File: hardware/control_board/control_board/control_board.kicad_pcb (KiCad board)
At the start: 4 copper layers, 140 parts, among them J1 USB_B, J2 Conn_02x08_Counter_Clockwise, J3 Conn_01x06_Pin, J4 Barrel_Jack_Switch, Q1 SS8550, Q2 AO3401A, SW1 SW_MEC_5G, SW2 SW_MEC_5G, U1 STM32F411CEUx, U2 M24C64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

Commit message: feat：调试接口预布局；USB接口预布局
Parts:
- added D9: 1N4007, Diode_SMD:D_SOD-123, F.Cu at (121.3, 43.7)
- added R30: 4.7kR, Resistor_SMD:R_0603_1608Metric, F.Cu at (117.7, 39.4)
- added R31: 4.7kR, Resistor_SMD:R_0603_1608Metric, F.Cu at (119.2, 39.4)
- TP11: value +1V -> +3.3V
- moved Q2 138.4 mm to (119.7, 93.6), turned to 180 degrees
- moved D3 135.4 mm to (122.9, 93.6), turned to -90 degrees
- moved BT1 133.0 mm to (110.5, 108.5), turned to -90 degrees
- moved R4 131.2 mm to (122.9, 97.5), turned to 90 degrees
- moved R10 117.7 mm to (154.9, 40.2)
- moved R11 117.7 mm to (154.9, 38.7)
- moved R9 117.7 mm to (154.9, 41.6)
- moved U2 117.7 mm to (149.3, 39.5)
- moved C6 117.7 mm to (151.0, 35.8)
- moved R8 106.6 mm to (176.9, 101.4)
- moved SW1 106.6 mm to (176.9, 94.9)
- moved C10 105.6 mm to (154.6, 107.4)
- moved C11 105.6 mm to (143.3, 102.2)
- moved C2 105.6 mm to (140.8, 114.1)
- moved C4 105.6 mm to (137.3, 106.3)
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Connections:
- D2 pad 1: GND -> /MCU/Debug_LED
- D2 pad 2: /MCU/Debug_LED -> Net-(D2-A)
- Q1 pad 1: /MCU/Buzzer -> Net-(Q1-B)
- R3 pad 1: /MCU/Debug_LED -> Net-(D2-A)
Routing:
- net /USB_D.USB_D+: track 0.00 -> 10.0 mm
- net /USB_D.USB_D-: track 0.00 -> 8.67 mm
- net VBUS: track 0.00 -> 1.63 mm
- net /USB_D.VBUS_Check: track 0.00 -> 1.49 mm

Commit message: feat：电源预布局
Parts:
- added J5: Conn_01x08, Connector_JST:JST_VH_B8P-VH_1x08_P3.96mm_Vertical, F.Cu at (37.0, 113.6)
- moved R26 130.1 mm to (-48.6, 53.0), turned to -90 degrees
- moved R24 129.6 mm to (-48.5, 49.2), turned to 90 degrees
- moved R27 128.4 mm to (-47.1, 56.4), turned to 90 degrees
- moved R25 128.2 mm to (-48.6, 56.0), turned to -90 degrees
- moved R22 121.2 mm to (-48.2, 94.5), turned to -90 degrees
- moved C50 120.8 mm to (-45.1, 46.6)
- moved R23 119.7 mm to (-46.7, 97.9), turned to 90 degrees
- moved C51 119.4 mm to (-42.1, 46.6), turned to 180 degrees
- moved R20 118.1 mm to (-48.1, 90.7), turned to 90 degrees
- moved R21 117.7 mm to (-48.2, 97.5), turned to -90 degrees
- moved C59 116.7 mm to (-44.9, 57.2)
- moved D2 116.7 mm to (190.3, 75.1)
- moved R3 116.7 mm to (193.6, 75.1)
- moved C58 116.4 mm to (-44.9, 55.7)
- moved C53 116.2 mm to (-49.3, 72.3)
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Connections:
- C15 pad 1: +17V -> V_{IN}
- C16 pad 2: +17V -> V_{IN}
- C17 pad 2: +17V -> V_{IN}
- C18 pad 2: +17V -> V_{IN}
- C37 pad 1: +17V -> V_{IN}
- C38 pad 2: +17V -> V_{IN}
- C39 pad 2: +17V -> V_{IN}
- C40 pad 2: +17V -> V_{IN}
- C41 pad 2: +17V -> V_{IN}
- C61 pad 2: +17V -> V_{IN}
- C62 pad 2: +17V -> V_{IN}
- C63 pad 2: +17V -> V_{IN}
- U3 pad 2: +17V -> V_{IN}
- U5 pad 2: +17V -> V_{IN}
- U7 pad 3: +17V -> V_{IN}
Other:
- board outline added: 100 x 100 mm

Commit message: feat：整版布局
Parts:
- C6, R10, R11, R9, U2: moved to B.Cu
- TP1: value SPI_CS -> CS
- TP2: value SPI_CLK -> CLK
- TP3: value SPI_MISO -> MISO
- TP4: value SPI_MOSI -> MOSI
- TP5: value IIC_SCL -> SCL
- TP6: value IIC_SDA -> SDA
- moved C5 134.5 mm to (110.7, 90.1), turned to 90 degrees
- moved SW2 132.3 mm to (111.6, 96.6), turned to 90 degrees
- moved R7 131.5 mm to (112.2, 90.1), turned to 90 degrees
- moved R10 131.2 mm to (92.6, 77.3), turned to 180 degrees
- moved R11 131.2 mm to (92.6, 75.8), turned to 180 degrees
- moved R9 131.2 mm to (92.6, 78.8), turned to 180 degrees
- moved R8 130.3 mm to (116.2, 90.1), turned to -90 degrees
- moved J3 129.5 mm to (83.2, 65.4)
- moved SW1 128.3 mm to (116.2, 96.5), turned to -90 degrees
- moved C6 123.5 mm to (96.5, 73.0), turned to 0 degrees
- moved C9 121.7 mm to (100.4, 86.0)
- moved C8 121.7 mm to (99.4, 85.0)
- moved C11 121.6 mm to (93.2, 88.7)
- moved C13 121.6 mm to (96.2, 97.0)
- moved R5 121.6 mm to (100.4, 99.1)
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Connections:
- U1 pad 31: /MCU/VBUS_Check -> /USB_D.VBUS_Check
- U1 pad 32: /MCU/USB_D- -> /USB_D.USB_D-
- U1 pad 33: /MCU/USB_D+ -> /USB_D.USB_D+
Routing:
- net /USB_D.USB_D-: track 8.67 -> 3.30 mm
- net /USB_D.USB_D+: track 10.0 -> 8.10 mm

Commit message: feat：MCU、USB、EEPROM、Debug布线
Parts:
- SW1: value SW_MEC_5G -> BOOT0
- SW2: value SW_MEC_5G -> NRST
- moved R30 15.6 mm to (111.2, 66.0)
- moved R31 15.6 mm to (111.2, 64.5)
- moved BZ1 15.6 mm to (111.2, 56.4)
- moved Q1 15.6 mm to (111.2, 61.7)
- moved D9 15.5 mm to (114.5, 62.5)
- moved R3 13.1 mm to (116.3, 73.5)
- moved D2 12.5 mm to (116.3, 75.0), turned to 180 degrees
- moved C5 11.4 mm to (115.7, 79.8)
- moved R7 11.4 mm to (117.2, 79.8)
- moved SW2 11.4 mm to (116.5, 86.3)
- moved R8 3.11 mm to (116.6, 93.2)
- moved SW1 3.11 mm to (116.6, 99.6)
- moved C23 2.23 mm to (32.6, 32.7)
- moved C25 2.23 mm to (27.7, 29.0)
- moved C26 2.23 mm to (27.7, 26.6)
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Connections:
- C61 pad 2: V_{IN} -> +17V
- C62 pad 2: V_{IN} -> +17V
- C63 pad 2: V_{IN} -> +17V
- U7 pad 3: V_{IN} -> +17V
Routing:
- net /MCU/NRST: track 0.00 -> 79.3 mm, vias 0 -> 2
- net /USB_D.USB_D-: track 3.30 -> 63.3 mm
- net /USB_D.USB_D+: track 8.10 -> 63.4 mm
- net /USB_D.VBUS_Check: track 1.49 -> 56.8 mm, vias 0 -> 2
- net /MCU/BOOT0: track 0.00 -> 33.8 mm, vias 0 -> 2
- net /MCU/Debug_RX: track 0.00 -> 31.2 mm, vias 0 -> 1
- net /MCU/Debug_TX: track 0.00 -> 29.8 mm, vias 0 -> 1
- net /MCU/SWDIO: track 0.00 -> 29.7 mm, vias 0 -> 1
- net /MCU/SWCLK: track 0.00 -> 29.1 mm, vias 0 -> 1
- net /MCU/Buzzer: track 0.00 -> 28.8 mm
- net /FPGA_Ctrl.Ctrl_SPI_CS: track 0.00 -> 24.7 mm
- net /FPGA_Ctrl.Ctrl_SPI_MISO: track 0.00 -> 24.5 mm
- net /FPGA_Ctrl.Ctrl_FPGA_NRST: track 0.00 -> 22.5 mm
- net /MCU/Debug_LED: track 0.00 -> 22.4 mm
- net +3.3V: track 2.32 -> 24.5 mm, vias 0 -> 9
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- added copper zone on F.Cu, net +3.3V
- added copper zone on B.Cu, net GND
- added copper zone on F.Cu, net GND
- added copper zone on In1.Cu, net GND
- added copper zone on F.Cu, net Net-(BT1-+)
- added copper zone on F.Cu, net Net-(BZ1-+)
- added copper zone on F.Cu, net Net-(D3-K)
- added copper zone on In2.Cu, net Net-(D3-K)
- added copper zone on F.Cu, net VBUS

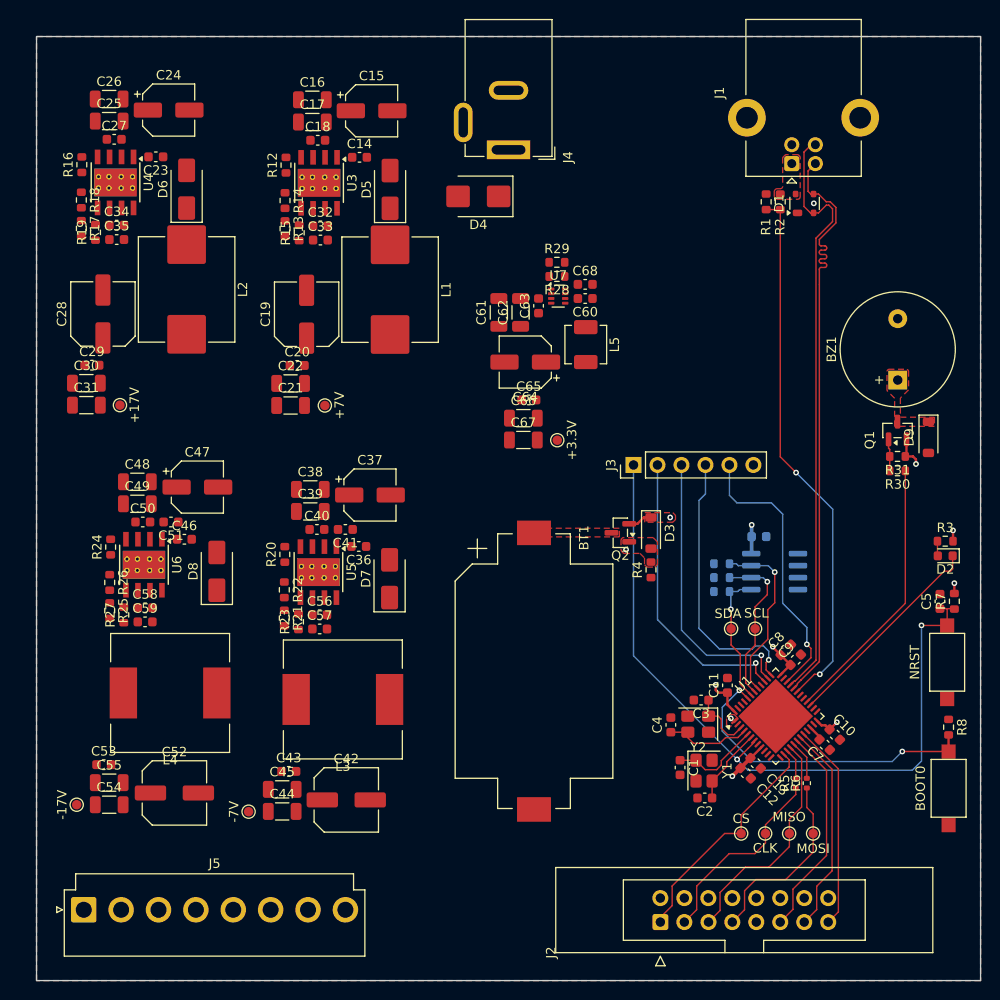
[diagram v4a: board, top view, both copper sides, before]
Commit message: feat：电源布线
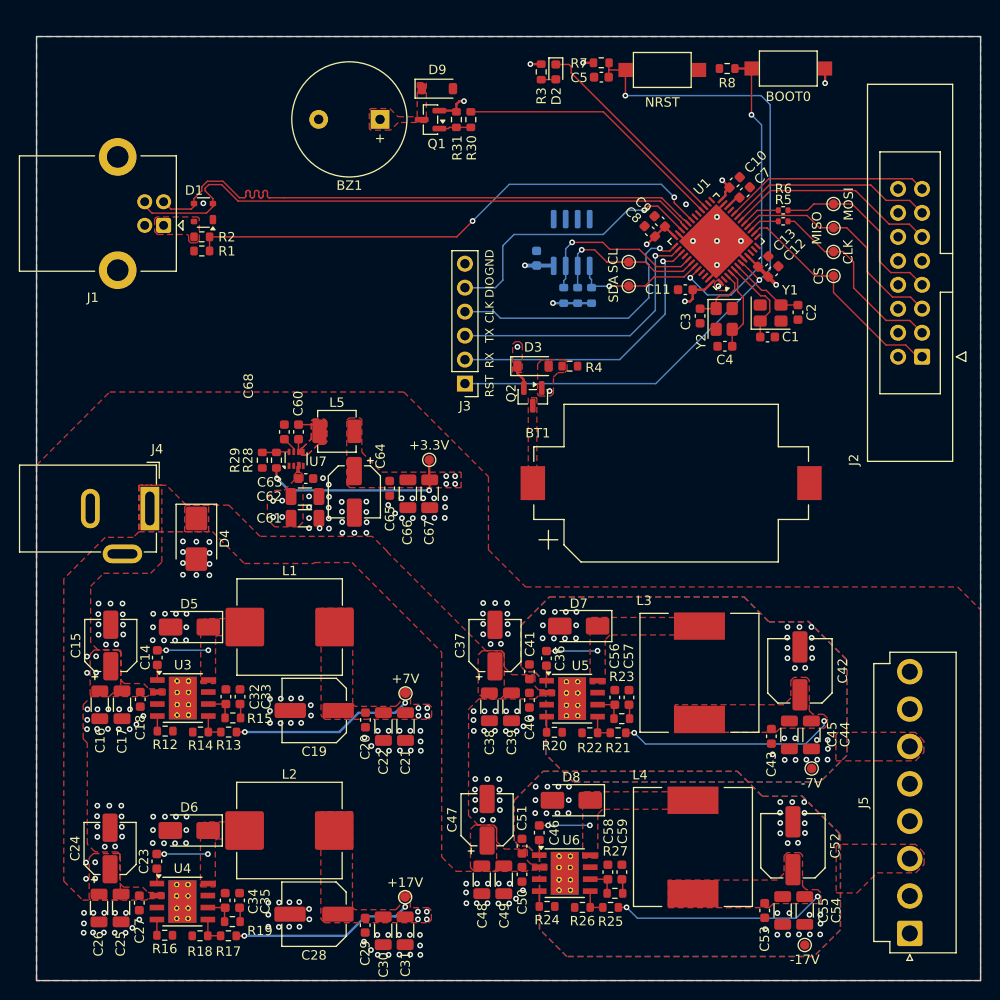
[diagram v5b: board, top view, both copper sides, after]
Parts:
- moved J5 87.5 mm to (112.5, 115.0), turned to 90 degrees
- moved C26 85.7 mm to (26.6, 112.3), turned to 90 degrees
- moved C25 83.4 mm to (29.0, 112.3), turned to 90 degrees
- moved R16 82.1 mm to (33.6, 115.2), turned to 180 degrees
- moved C27 80.9 mm to (30.9, 111.8), turned to 90 degrees
- moved R18 78.9 mm to (37.3, 115.3), turned to 0 degrees
- moved TP10 78.5 mm to (101.4, 116.2), turned to 0 degrees
- moved C24 78.5 mm to (27.8, 106.0), turned to 90 degrees
- moved SW1 78.1 mm to (99.6, 23.4), turned to 0 degrees
- moved R17 76.5 mm to (40.3, 115.3), turned to 0 degrees
- moved U4 76.5 mm to (35.5, 111.6), turned to 0 degrees
- moved C23 74.6 mm to (32.7, 107.4), turned to -90 degrees
- moved C54 74.5 mm to (101.4, 112.6), turned to 90 degrees
- moved R19 74.4 mm to (40.7, 113.8), turned to 180 degrees
- moved R8 73.6 mm to (93.2, 23.4), turned to 0 degrees
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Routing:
- net GND: track 0.00 -> 62.2 mm, vias 1 -> 218
- net +3.3V: track 24.5 -> 51.2 mm, vias 9 -> 17
- net +17V: track 0.00 -> 19.8 mm, vias 0 -> 10
- net +7V: track 0.00 -> 19.2 mm, vias 0 -> 6
- net Net-(D7-K): track 0.00 -> 5.42 mm, vias 0 -> 2
- net Net-(D6-K): track 0.00 -> 5.42 mm, vias 0 -> 2
- net Net-(D5-K): track 0.00 -> 5.41 mm, vias 0 -> 2
- net Net-(D8-K): track 0.00 -> 5.36 mm, vias 0 -> 2
- net Net-(U6-COMP): track 0.11 -> 3.50 mm
- net Net-(U3-COMP): track 0.00 -> 3.37 mm
- net Net-(U4-COMP): track 0.00 -> 3.34 mm
- net Net-(U5-COMP): track 0.00 -> 3.34 mm
- net Net-(U7-SW): track 0.00 -> 3.33 mm
- net /POWER/FB_+17V: track 0.00 -> 3.08 mm
- net /POWER/FB_-17V: track 0.00 -> 3.06 mm
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- added copper zone on F.Cu, net (none)
- added copper zone on F.Cu, net +17V
- added copper zone on In2.Cu, net +17V
- added copper zone on In2.Cu, net +3.3V
- added copper zone on F.Cu, net +7V
- added copper zone on In2.Cu, net +7V
- added copper zone on B.Cu, net -17V
- added copper zone on F.Cu, net -17V
- added copper zone on B.Cu, net -7V
- added copper zone on F.Cu, net -7V
- added copper zone on F.Cu, net Net-(D5-K)
- added copper zone on F.Cu, net Net-(D6-K)
- added copper zone on F.Cu, net Net-(D7-K)
- added copper zone on F.Cu, net Net-(D8-K)
- added copper zone on F.Cu, net Net-(U7-SW)
- added copper zone on F.Cu, net V_{IN}
- added copper zone on In2.Cu, net V_{IN}
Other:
- board text added: "CLK"
- board text added: "DIO"
- board text added: "GND"
- board text added: "RST"
- board text added: "RX"
- board text added: "TX"

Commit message: feat：添加缝合过孔
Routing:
- net GND: vias 218 -> 322
- net -7V: vias 32 -> 40
- net -17V: vias 32 -> 41
